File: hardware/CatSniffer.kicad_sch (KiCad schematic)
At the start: 76 parts, among them J1 Antenna, J2 Conn_01x06_Female, J3 Conn_01x06_Female, P1 USB_C_Plug_USB2.0, SW1 SW, U1 AP2112K-3.3, U2 RFSW8006QTR7, U3 ATSAMD21E18A, U4 0900PC15A0036, U5 0900FM15D0039, U6 SW409, U7 SX1262IMLTRT, U8 CC1352P1F3RGZT, Y1 48MHz, Y2 32.768kHz, Y3 32Mhz

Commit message: update version
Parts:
- removed C28, C30: 47pF, Capacitor_SMD:C_0603_1608Metric, symbol CatSniffer-rescue:C-Device-CatStick-rescue-CatSniffer-rescue
- U6: value SW409 -> PE42421; footprint CatSniffer:SW409 -> Package_TO_SOT_SMD:SOT-363_SC-70-6; LCSC# C391968 -> -; manf# SW409 -> PE42421SCAA-Z; provedor LCSC -> Mouser
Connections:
- net SW_RFI: now also U6.3 (RF2)
- net SW_RFO: now also U6.1 (RF1)
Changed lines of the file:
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@@
     (title "CatSniffer")
     (date "2021-04-11")
-    (rev "1.0")
+    (rev "2.0")
     (company "ElectronicCats")
     (comment 3 "Edgar Herrera")
@@
     (stroke (width 0) (type default) (color 0 0 0 0))
   )
-  (wire (pts (xy 486.664 186.309) (xy 488.188 186.309))
-    (stroke (width 0) (type default) (color 0 0 0 0))
-  )
   (wire (pts (xy 303.403 50.673) (xy 316.103 50.673))
     (stroke (width 0) (type default) (color 0 0 0 0))
@@
     (stroke (width 0) (type default) (color 0 0 0 0))
   )
+  (wire (pts (xy 486.664 186.309) (xy 499.618 186.309))
+    (stroke (width 0) (type default) (color 0 0 0 0))
+  )
   (wire (pts (xy 314.198 192.024) (xy 312.039 192.024))
     (stroke (width 0) (type default) (color 0 0 0 0))
@@
     (stroke (width 0) (type default) (color 0 0 0 0))
   )
+  (wire (pts (xy 486.918 181.229) (xy 499.618 181.229))
+    (stroke (width 0) (type default) (color 0 0 0 0))
+  )
   (wire (pts (xy 548.64 166.751) (xy 552.069 166.751))
     (stroke (width 0) (type default) (color 0 0 0 0))
@@
     (stroke (width 0) (type default) (color 0 0 0 0))
   )
-  (wire (pts (xy 495.554 181.229) (xy 499.618 181.229))
-    (stroke (width 0) (type default) (color 0 0 0 0))
-  )
   (wire (pts (xy 357.124 169.164) (xy 357.124 164.719))
     (stroke (width 0) (type default) (color 0 0 0 0))
   )
-  (wire (pts (xy 495.808 186.309) (xy 499.618 186.309))
-    (stroke (width 0) (type default) (color 0 0 0 0))
-  )
   (polyline (pts (xy 531.114 99.187) (xy 531.114 111.506))
     (stroke (width 0) (type default) (color 0 0 0 0))
@@
     (stroke (width 0) (type default) (color 0 0 0 0))
   )
-  (wire (pts (xy 486.918 181.229) (xy 487.934 181.229))
-    (stroke (width 0) (type default) (color 0 0 0 0))
-  )
   (wire (pts (xy 177.038 166.37) (xy 172.339 166.37))
     (stroke (width 0) (type default) (color 0 0 0 0))
@@
     (pin "1")
   )
-  (symbol (lib_id "CatSniffer-rescue:C-Device-CatStick-rescue-CatSniffer-rescue") (at 491.744 181.229 90) (unit 1)
-    (in_bom yes) (on_board yes)
-    (property "Reference" "C28" (id 0) (at 496.062 177.546 90)
-      (effects (font (size 1.27 1.27)) (justify left))
-    )
-    (property "Value" "47pF" (id 1) (at 497.459 179.705 90)
-      (effects (font (size 1.27 1.27)) (justify left))
-    )
-    (property "Footprint" "Capacitor_SMD:C_0603_1608Metric" (id 2) (at 495.554 180.2638 0)
-      (effects (font (size 1.27 1.27)) hide)
-    )
-    (property "Datasheet" "" (id 3) (at 491.744 181.229 0))
-    (property "provedor" "LCSC" (id 4) (at 491.744 181.229 0)
-      (effects (font (size 1.27 1.27)) hide)
-    )
-    (property "LCSC#" "C519486" (id 5) (at 491.744 181.229 0)
-      (effects (font (size 1.27 1.27)) hide)
-    )
-    (property "manf#" "CC0603FRNPO9BN470" (id 6) (at 491.744 181.229 0)
-      (effects (font (size 1.27 1.27)) hide)
-    )
-    (pin "1")
-    (pin "2")
-  )
-  (symbol (lib_id "CatSniffer-rescue:C-Device-CatStick-rescue-CatSniffer-rescue") (at 491.998 186.309 90) (unit 1)
-    (in_bom yes) (on_board yes)
-    (property "Reference" "C30" (id 0) (at 497.332 187.452 90)
-      (effects (font (size 1.27 1.27)) (justify left))
-    )
-    (property "Value" "47pF" (id 1) (at 497.967 189.357 90)
-      (effects (font (size 1.27 1.27)) (justify left))
-    )
-    (property "Footprint" "Capacitor_SMD:C_0603_1608Metric" (id 2) (at 495.808 185.3438 0)
-      (effects (font (size 1.27 1.27)) hide)
-    )
-    (property "Datasheet" "" (id 3) (at 491.998 186.309 0))
-    (property "provedor" "LCSC" (id 4) (at 491.998 186.309 0)
-      (effects (font (size 1.27 1.27)) hide)
-    )
-    (property "LCSC#" "C519486" (id 5) (at 491.998 186.309 0)
-      (effects (font (size 1.27 1.27)) hide)
-    )
-    (property "manf#" "CC0603FRNPO9BN470" (id 6) (at 491.998 186.309 0)
-      (effects (font (size 1.27 1.27)) hide)
-    )
-    (pin "1")
-    (pin "2")
-  )
   (symbol (lib_id "CatSniffer-rescue:C-Device-CatStick-rescue-CatSniffer-rescue") (at 539.369 171.831 0) (unit 1)
     (in_bom yes) (on_board yes)
@@
     (in_bom yes) (on_board yes)
     (property "Reference" "U6" (id 0) (at 509.778 175.514 0))
-    (property "Value" "SW409" (id 1) (at 509.778 177.8254 0))
-    (property "Footprint" "CatSniffer:SW409" (id 2) (at 509.778 183.769 0)
+    (property "Value" "PE42421" (id 1) (at 509.778 177.8254 0))
+    (property "Footprint" "Package_TO_SOT_SMD:SOT-363_SC-70-6" (id 2) (at 509.778 183.769 0)
       (effects (font (size 1.27 1.27)) hide)
     )
-    (property "Datasheet" "https://datasheet.lcsc.com/lcsc/1912111437_RFIC-SW409_C391968.pdf" (id 3) (at 509.778 183.769 0)
+    (property "Datasheet" "https://www.mouser.mx/datasheet/2/281/pe42421ds-1671115.pdf" (id 3) (at 509.778 183.769 0)
       (effects (font (size 1.27 1.27)) hide)
     )
-    (property "LCSC#" "C391968" (id 4) (at 509.778 186.309 0)
+    (property "LCSC#" "-" (id 4) (at 509.778 186.309 0)
       (effects (font (size 1.27 1.27)) hide)
     )
-    (property "manf#" "SW409" (id 5) (at 509.778 186.309 0)
+    (property "manf#" "PE42421SCAA-Z" (id 5) (at 509.778 186.309 0)
       (effects (font (size 1.27 1.27)) hide)
     )
-    (property "provedor" "LCSC" (id 6) (at 509.778 186.309 0)
+    (property "provedor" "Mouser" (id 6) (at 509.778 186.309 0)
       (effects (font (size 1.27 1.27)) hide)
     )
@@
       (reference "C27") (unit 1) (value "100pF") (footprint "Capacitor_SMD:C_0603_1608Metric")
     )
-    (path "/00000000-0000-0000-0000-000060977a2f"
-      (reference "C28") (unit 1) (value "47pF") (footprint "Capacitor_SMD:C_0603_1608Metric")
-    )
     (path "/00000000-0000-0000-0000-000060ea4035"
       (reference "C29") (unit 1) (value "0.1uF") (footprint "Capacitor_SMD:C_0603_1608Metric")
     )
-    (path "/00000000-0000-0000-0000-000060977e80"
-      (reference "C30") (unit 1) (value "47pF") (footprint "Capacitor_SMD:C_0603_1608Metric")
-    )
     (path "/00000000-0000-0000-0000-000060cf4963"
       (reference "C31") (unit 1) (value "1nF") (footprint "Capacitor_SMD:C_0603_1608Metric")
@@
     )
     (path "/00000000-0000-0000-0000-000060fa8e32"
-      (reference "U6") (unit 1) (value "SW409") (footprint "CatSniffer:SW409")
+      (reference "U6") (unit 1) (value "PE42421") (footprint "Package_TO_SOT_SMD:SOT-363_SC-70-6")
     )
     (path "/00000000-0000-0000-0000-000060bf3807"

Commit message: Init RP2040
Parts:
- added C? (x2): 1uF, symbol Device:C_Small
- added C? (x2): 27pF, symbol Device:C_Small
- added C? (x9): 0.1uF, symbol Device:C_Small
- added R? (x2): 27, symbol Device:R_Small
- added R?: 1k, symbol Device:R_Small
- added U?: RP2040, Package_DFN_QFN:QFN-56-1EP_7x7mm_P0.4mm_EP3.2x3.2mm, symbol MCU_RaspberryPi:RP2040
- added Y?: 12MHz, symbol Device:Crystal_GND2_Small
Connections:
- net +3V3: now also C?.1, C?.1, C?.1, C?.1, C?.1, C?.1, C?.1, C?.1, U?.1 (IOVDD), U?.10 (IOVDD), U?.22 (IOVDD), U?.33 (IOVDD), U?.42 (IOVDD), U?.43 (ADC_AVDD), U?.44 (VREG_IN), U?.48 (USB_VDD), U?.49 (IOVDD)
- net D+: now also R?.1
- net D-: now also R?.1
- net GND: now also C?.2, C?.2, C?.2, C?.2, C?.2, C?.2, C?.2, C?.2, C?.2, C?.2, C?.2, C?.2, C?.2, U?.19 (TESTEN), U?.57 (GND), Y?.2
- new net: C?.1, R?.1, Y?.3
- new net: R?.2, U?.47 (USB_DP)
- new net: C?.1, U?.20 (XIN), Y?.1
- new net: R?.2, U?.21 (XOUT)
- new net: R?.2, U?.46 (USB_DM)
- new net +1V2: C?.1, C?.1, C?.1, U?.23 (DVDD), U?.45 (VREG_VOUT), U?.50 (DVDD)
- new net QSPI_SCK: U?.52 (QSPI_SCLK)
- new net QSPI_SD0: U?.53 (QSPI_SD0)
- new net QSPI_SD1: U?.55 (QSPI_SD1)
- new net QSPI_SD2: U?.54 (QSPI_SD2)
- new net QSPI_SD3: U?.51 (QSPI_SD3)
- new net QSPI_SS: U?.56 (QSPI_SS)
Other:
- moved on the sheet: C3, C4, C5, J2, U3

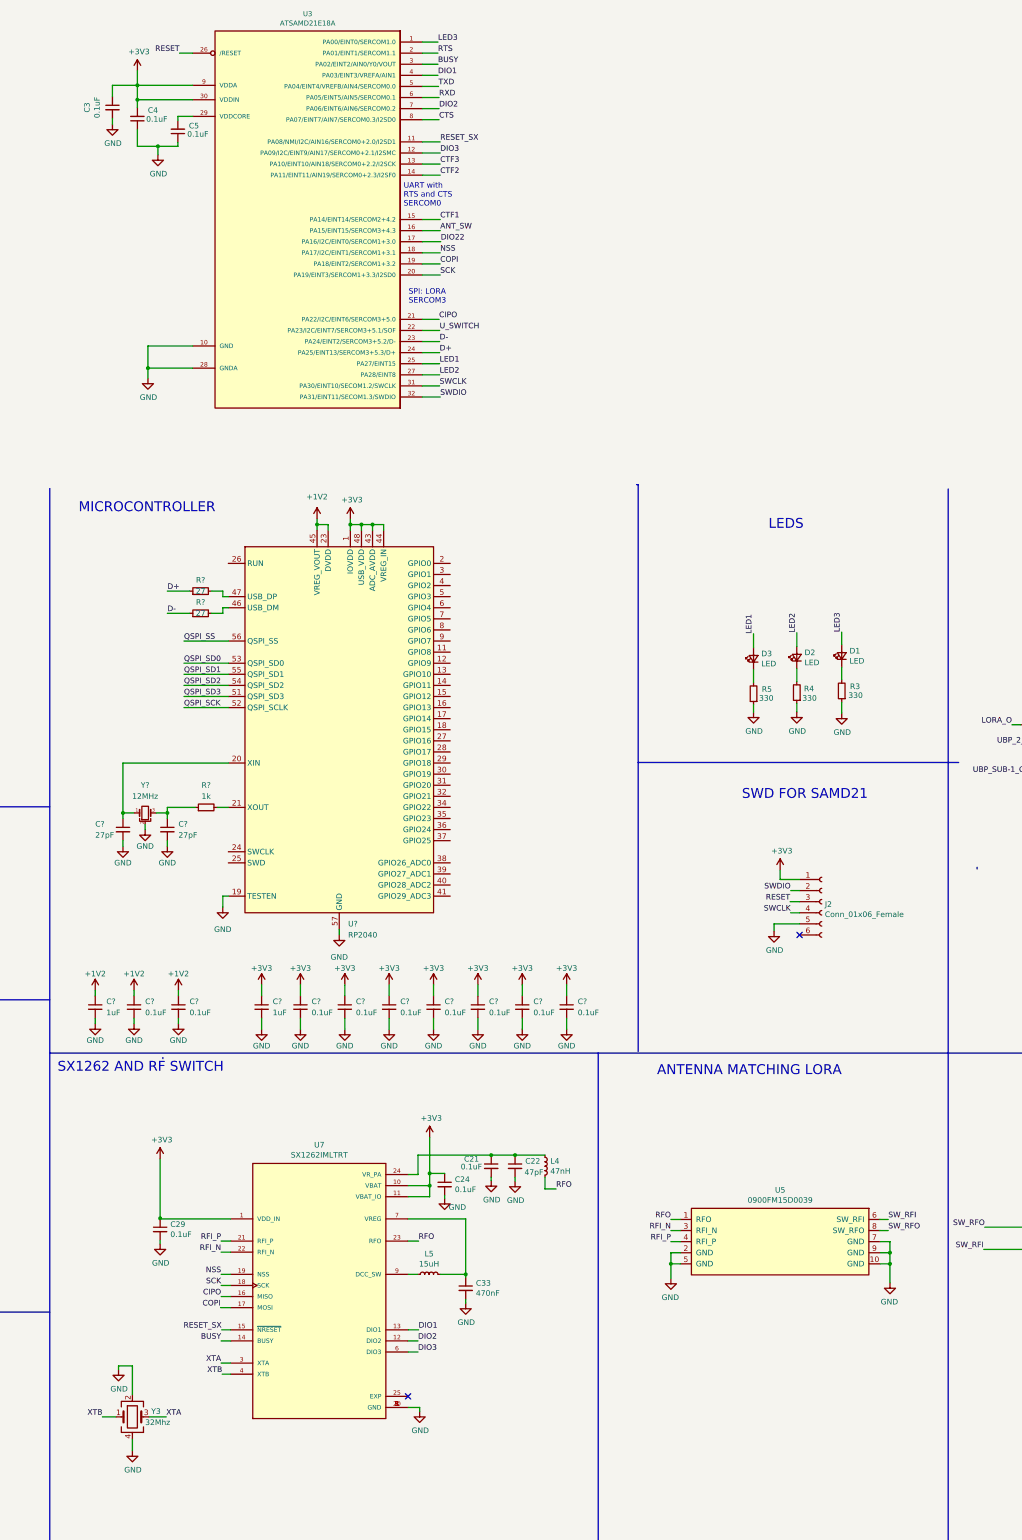
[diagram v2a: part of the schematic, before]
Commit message: Change RP2040
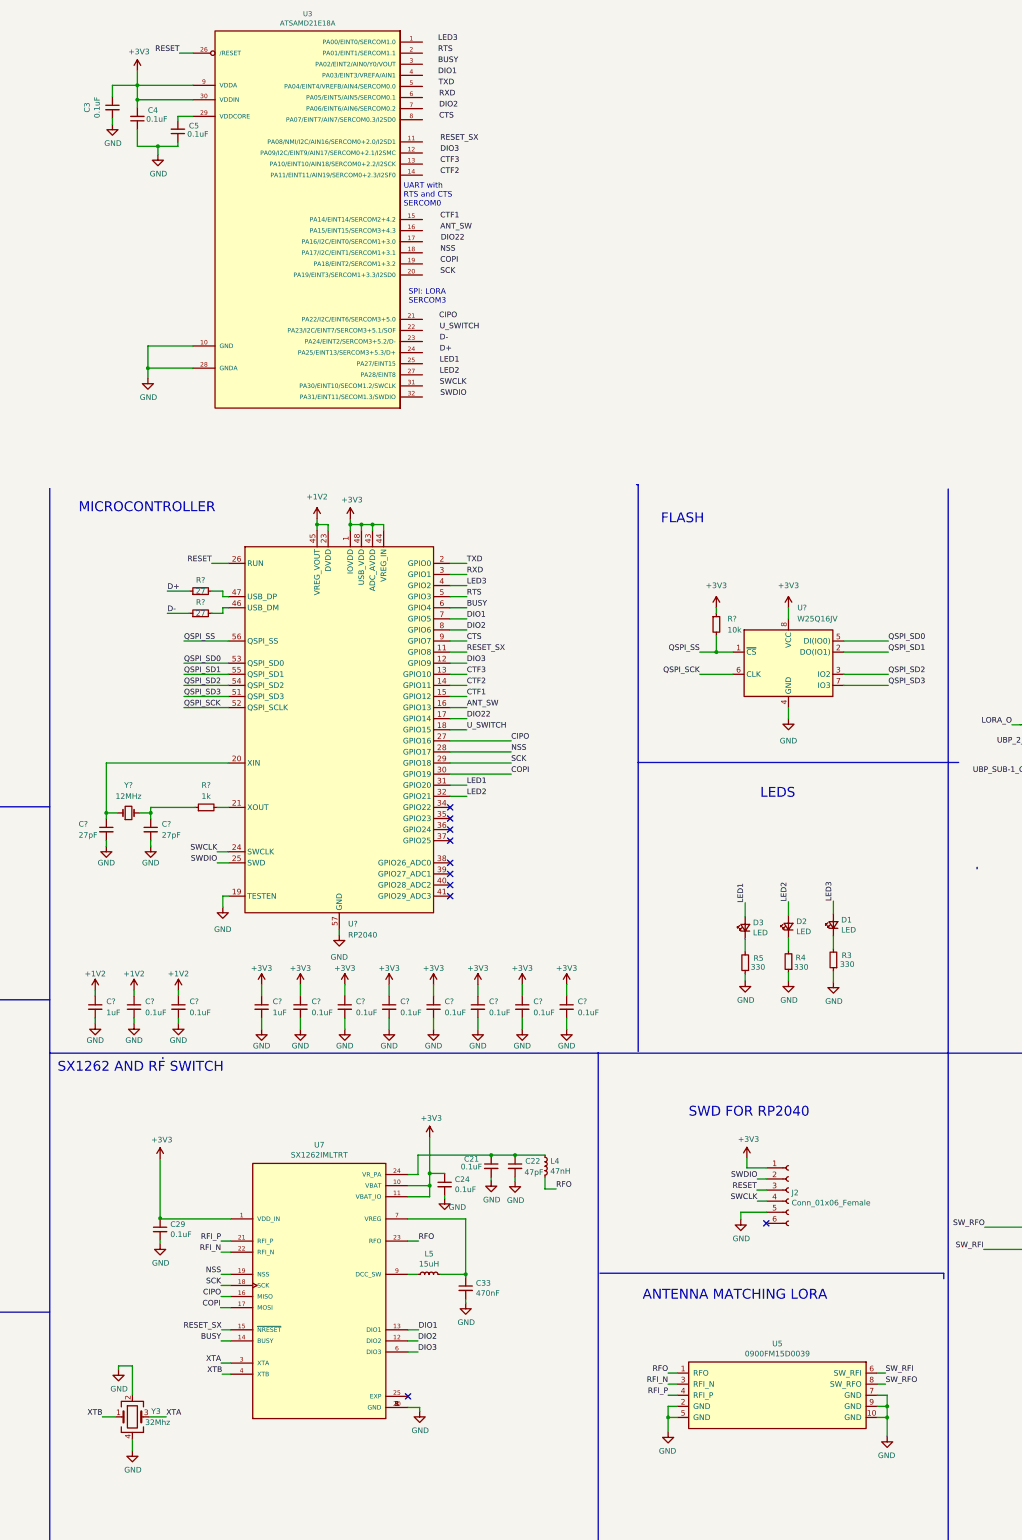
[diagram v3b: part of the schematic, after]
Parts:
- removed Y?: 12MHz, symbol Device:Crystal_GND2_Small
- added R?: 10k, symbol Device:R_Small
- added U?: W25Q16JV, Package_SO:SOIC-8_5.23x5.23mm_P1.27mm, symbol Memory_Flash:W25Q128JVS
- added Y?: 12MHz, symbol Device:Crystal_Small
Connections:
- net +3V3: now also R?.1, U?.8 (VCC)
- net ANT_SW: now also U?.16 (GPIO13); no longer U3.16 (PA15/EINT15/SERCOM3+4.3)
- net BOOT: now also U?.9 (GPIO7); no longer U3.8 (PA07/EINT7/AIN7/SERCOM0.3/I2SD0)
- net BUSY: now also U?.6 (GPIO4); no longer U3.3 (PA02/EINT2/AIN0/Y0/VOUT)
- net CIPO: now also U?.27 (GPIO16); no longer U3.21 (PA22/I2C/EINT6/SERCOM3+5.0)
- net COPI: now also U?.30 (GPIO19); no longer U3.19 (PA18/EINT2/SERCOM1+3.2)
- net CTF1: now also U?.15 (GPIO12); no longer U3.15 (PA14/EINT14/SERCOM2+4.2)
- net CTF2: now also U?.14 (GPIO11); no longer U3.14 (PA11/EINT11/AIN19/SERCOM0+2.3/I2SF0)
- net CTF3: now also U?.13 (GPIO10); no longer U3.13 (PA10/EINT10/AIN18/SERCOM0+2.2/I2SCK)
- net D+: no longer U3.24 (PA25/EINT13/SERCOM3+5.3/D+)
- net D-: no longer U3.23 (PA24/EINT2/SERCOM3+5.2/D-)
- net DIO1: now also U?.7 (GPIO5); no longer U3.4 (PA03/EINT3/VREFA/AIN1)
- net DIO2: now also U?.8 (GPIO6); no longer U3.7 (PA06/EINT6/AIN6/SERCOM0.2)
- net DIO22: now also U?.17 (GPIO14); no longer U3.17 (PA16/I2C/EINT0/SERCOM1+3.0)
- net DIO3: now also U?.12 (GPIO9); no longer U3.12 (PA09/I2C/EINT9/AIN17/SERCOM0+2.1/I2SMC)
- net GND: now also U?.4 (GND)
- net LED1: now also U?.31 (GPIO20); no longer U3.25 (PA27/EINT15)
- net LED2: now also U?.32 (GPIO21); no longer U3.27 (PA28/EINT8)
- net LED3: now also U?.4 (GPIO2); no longer U3.1 (PA00/EINT0/SERCOM1.0)
- net NSS: now also U?.28 (GPIO17); no longer U3.18 (PA17/I2C/EINT1/SERCOM1+3.1)
- net QSPI_SCK: now also U?.6 (CLK)
- net QSPI_SD0: now also U?.5 (DI(IO0))
- net QSPI_SD1: now also U?.2 (DO(IO1))
- net QSPI_SD2: now also U?.3 (IO2)
- net QSPI_SD3: now also U?.7 (IO3)
- net QSPI_SS: now also R?.2, U?.1 (~{CS})
- net RESET: now also U?.26 (RUN)
- net RESET_CC: now also U?.5 (GPIO3); no longer U3.2 (PA01/EINT1/SERCOM1.1)
- net RESET_SX: now also U?.11 (GPIO8); no longer U3.11 (PA08/NMI/I2C/AIN16/SERCOM0+2.0/I2SD1)
- net RXD: now also U?.3 (GPIO1); no longer U3.6 (PA05/EINT5/AIN5/SERCOM0.1)
- net SCK: now also U?.29 (GPIO18); no longer U3.20 (PA19/EINT3/SERCOM1+3.3/I2SD0)
- net SWCLK: now also U?.24 (SWCLK); no longer U3.31 (PA30/EINT10/SECOM1.2/SWCLK)
- net SWDIO: now also U?.25 (SWD); no longer U3.32 (PA31/EINT11/SECOM1.3/SWDIO)
- net TXD: now also U?.2 (GPIO0); no longer U3.5 (PA04/EINT4/VREFB/AIN4/SERCOM0.0)
- net U_SWITCH: now also U?.18 (GPIO15); no longer U3.22 (PA23/I2C/EINT7/SERCOM3+5.1/SOF)
- net at C?.1, R?.1: now also Y?.2
- net at C?.1, U?.20 (XIN): now also Y?.1
- no-connect marks 26 -> 34
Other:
- note added: "FLASH"
- note added: "SWD FOR RP2040"
- note removed: "SWD FOR SAMD21"
- moved on the sheet: C?, D1, D2, D3, J2, R3, R4, R5, U5
